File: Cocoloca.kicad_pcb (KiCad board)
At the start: 2 copper layers, 38.1 x 54.6 mm, 8 parts, among them J0 Conn_01x03_Male, J1 Conn_01x03_Male, J2 Conn_01x03_Male, U1 MC6847T1, U2 74LS157

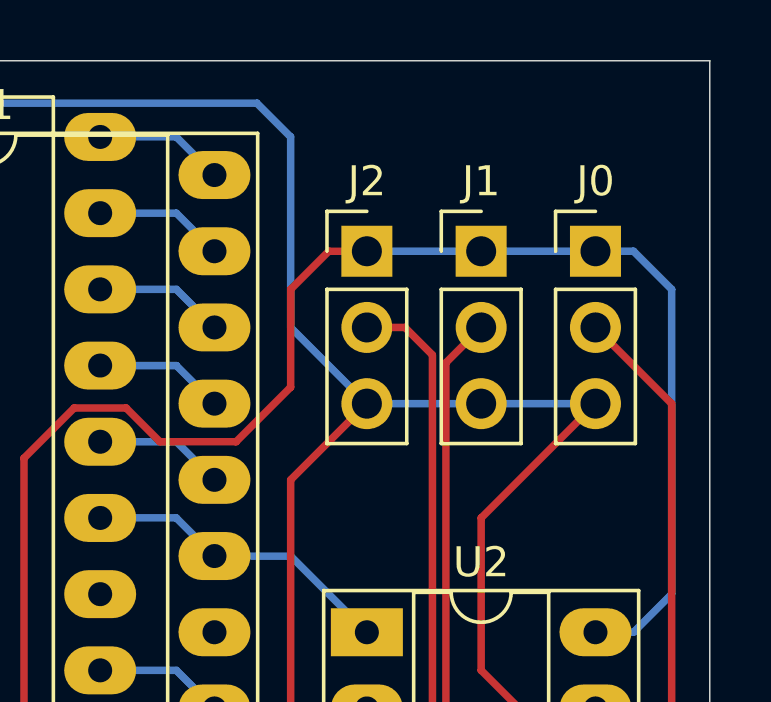
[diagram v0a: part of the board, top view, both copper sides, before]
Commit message: Gerbers cleaned up
Added missing edge cuts for Coco1 plug. Added dxf graphic files and cleaned up gerber plots as per board house production specs.
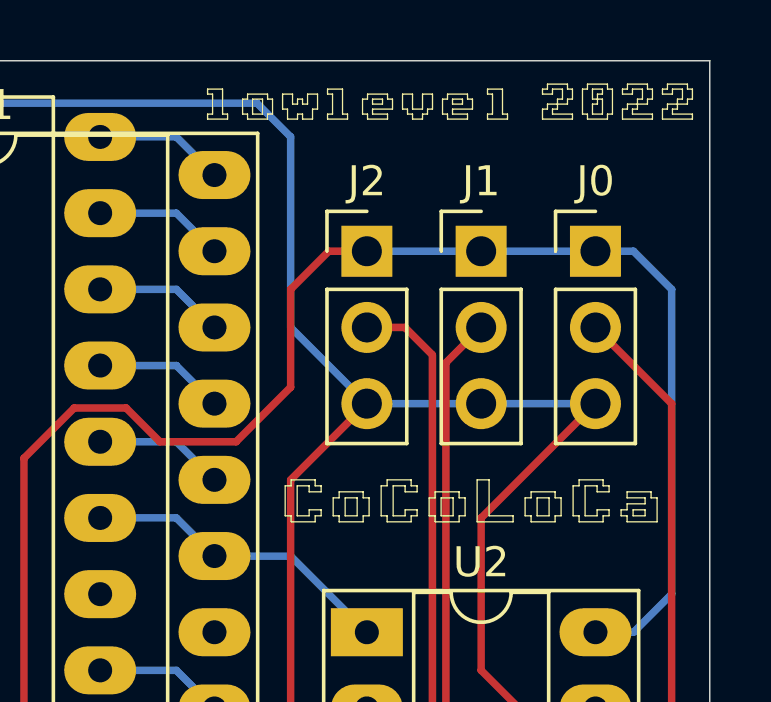
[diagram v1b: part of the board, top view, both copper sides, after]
